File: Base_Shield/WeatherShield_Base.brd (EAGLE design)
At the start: 90.3 x 67.3 mm, 78 parts, among them Q1 BSS138, Q2 BSS138, U1 DS3231SN, U2 LT3652, U4 MPL3115A2LGA8, U5 HTU21D

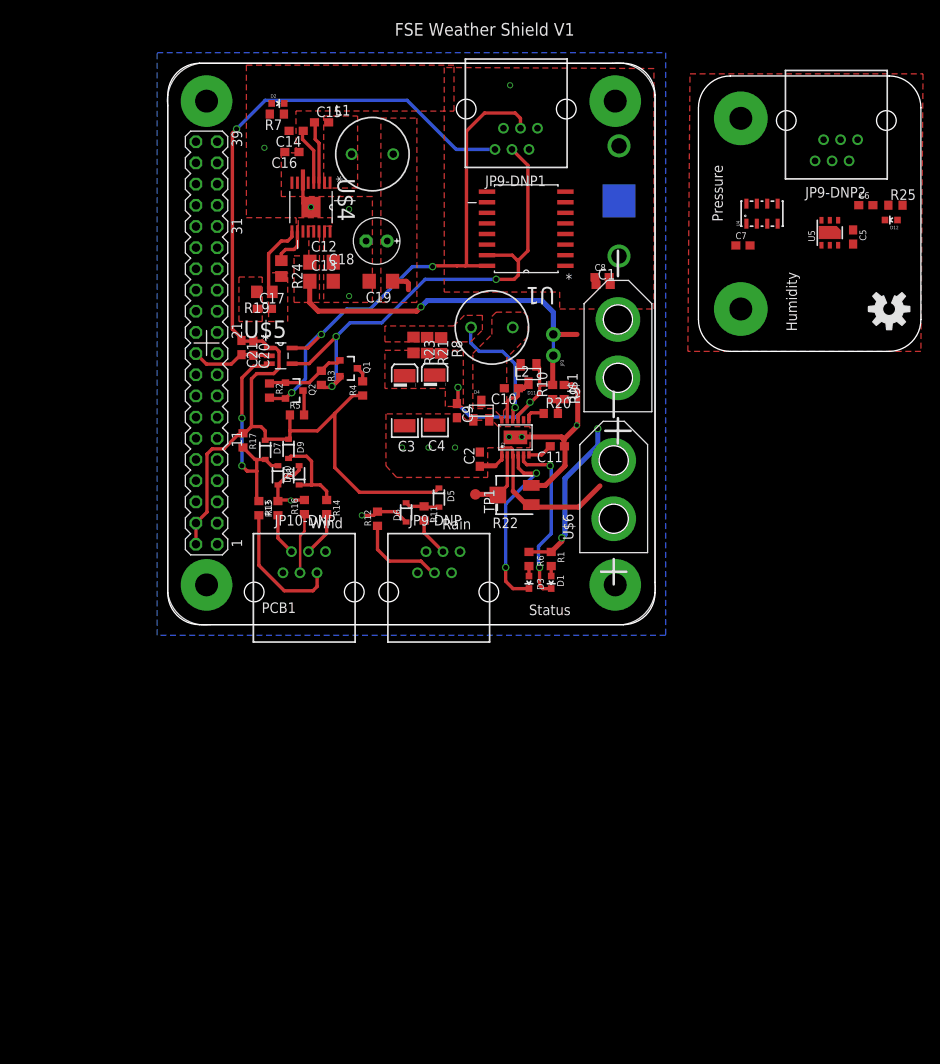
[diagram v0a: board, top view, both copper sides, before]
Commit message: WeatherShield v1
Restructuration des Fichiers
Division en Air et Base Board
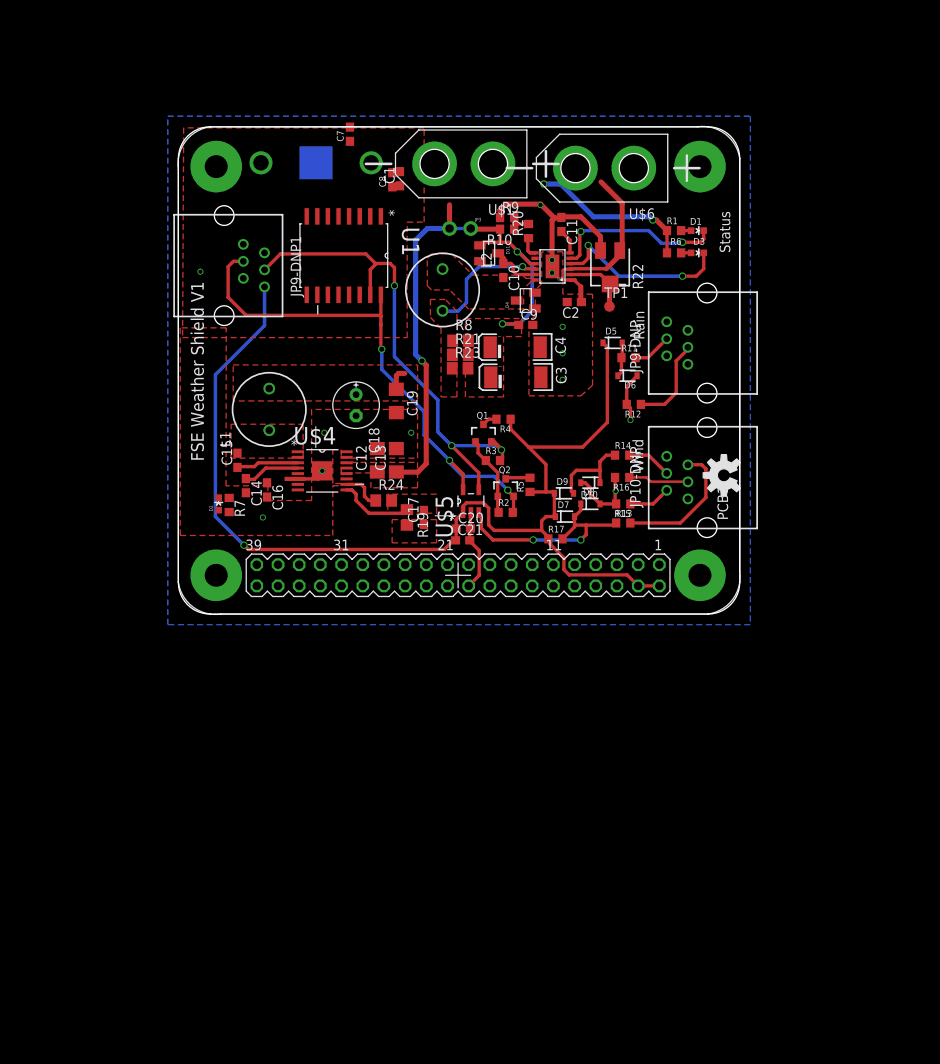
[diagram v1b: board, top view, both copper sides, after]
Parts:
- removed C5, C6: 0.1uF, rcl:C0603
- removed D12: AirBoard status led, SparkFun:LED-0603
- removed JP9-DNP2: RJ11-BUCHSE, FSEWeatherShield:RJ11-STECKER
- removed R25: 1K, rcl:R0603
- removed U4: MPL3115A2LGA8, SparkFun-Sensors:LGA8
- removed U5: HTU21D, SparkFun-Sensors:HTU21D
- moved JP10-DNP 61.9 mm to (70.7, 11.5), turned to 90 degrees
- moved PCB1 60.5 mm to (68.6, 59.7), turned to 180 degrees
- moved JP9-DNP 53.3 mm to (70.7, 27.7), turned to 90 degrees
- moved JP9-DNP1 50.7 mm to (0.76, 49.1), turned to 270 degrees
- moved C7 49.0 mm to (21.8, 58.8), turned to 90 degrees
- moved D2 48.5 mm to (6.10, 14.5), turned to 0 degrees
- moved R7 47.2 mm to (7.37, 14.4), turned to 270 degrees
- moved D1 45.7 mm to (63.5, 47.2), turned to 270 degrees
- moved D3 44.4 mm to (63.5, 44.6), turned to 270 degrees
- moved R13 43.7 mm to (54.6, 12.2), turned to 0 degrees
- moved C14 43.0 mm to (9.37, 16.7), turned to 270 degrees
- moved U$6 42.1 mm to (55.9, 54.7), turned to 180 degrees
- moved R1 42.0 mm to (60.7, 47.2), turned to 0 degrees
- moved C15 41.7 mm to (8.36, 19.7), turned to 90 degrees
- moved R15 41.4 mm to (54.6, 14.5), turned to 180 degrees
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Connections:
- removed net INT-PRESSURE: U4.6
- removed net N$28: D12.A, R25.2
- removed net N$5: C6.1, U4.2
- removed net STAT1: R25.1
- net 3.3V: no longer C5.1, JP9-DNP2.2, U4.1, U4.4, U5.VDD
- net 5V: no longer JP9-DNP2.1
- net GND: no longer C5.2, C6.2, D12.C, JP9-DNP2.5, JP9-DNP2.6, U4.3, U5.7, U5.GND
- net HV_SCL: now also PCB1.5
- net HV_SDA: now also PCB1.3
- net SCL: no longer JP9-DNP2.4, U4.8, U5.SCK
- net SDA: no longer JP9-DNP2.3, U4.7, U5.DATA
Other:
- board size 90.3 x 67.3 mm -> 67.3 x 58.4 mm
- board text removed: "Humidity"
- board text removed: "Pressure"

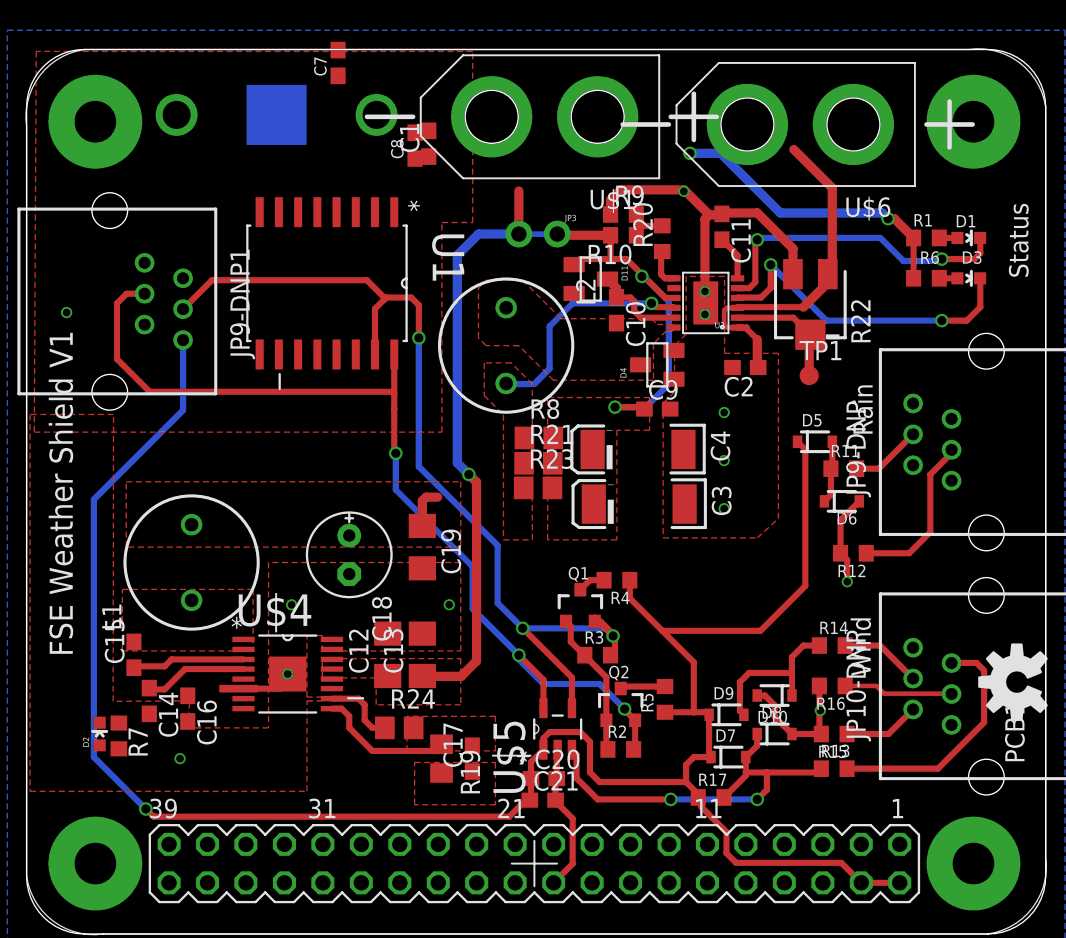
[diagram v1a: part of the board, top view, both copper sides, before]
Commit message: WeatherShield v1
First attempt almost done
GPIO routing is missing
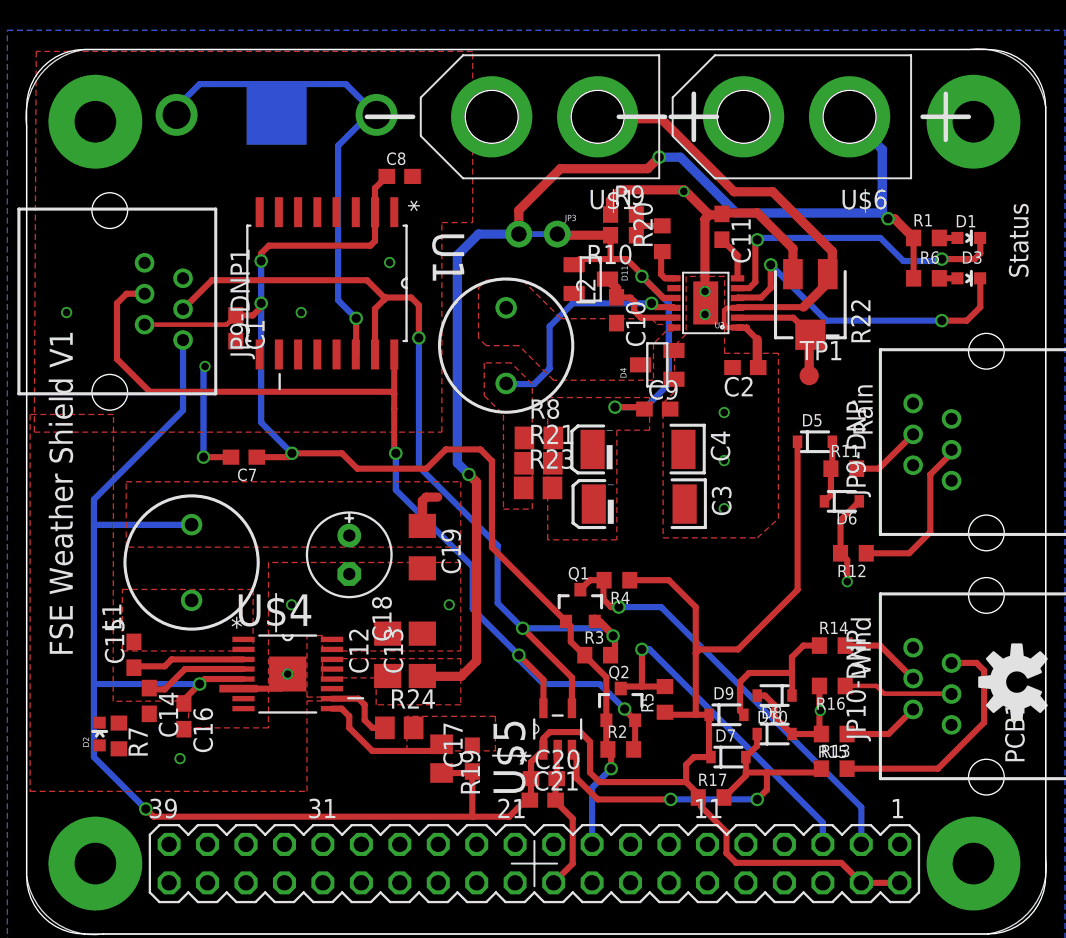
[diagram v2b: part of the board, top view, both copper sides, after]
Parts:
- moved C7 26.8 mm to (15.6, 32.8), turned to 180 degrees
- moved C1 17.6 mm to (15.1, 41.3), turned to 270 degrees
- moved C8 2.27 mm to (25.9, 51.3), turned to 0 degrees
- moved C16 0.57 mm to (11.7, 15.6)
- moved U$6 0.57 mm to (55.6, 55.2)
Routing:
- net 3.3V: track 9.63 -> 81.0 mm, vias 0 -> 4
- net N$6: track 0.00 -> 32.9 mm, vias 0 -> 1
- net HV_SDA: track 1.82 -> 28.3 mm, vias 0 -> 1
- net 5V: track 136.6 -> 159.4 mm, vias 1 -> 2
- net HV_SCL: track 2.98 -> 23.6 mm, vias 0 -> 1
- net V_BATT: track 58.6 -> 77.2 mm
- net VIN: track 23.4 -> 34.8 mm
- net GND: track 55.2 -> 63.1 mm, vias 13 -> 17
- added copper zone on layer 1, net 5V
- removed copper zone on layer 1, net +5V

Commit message: WeatherShield_v1
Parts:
- removed U$5: MCP3221A5T-E/OT, FSEWeatherShield:SOT95P270X145-5N
- added C5: 0.1uF, rcl:C0603
- added JP1, JP2, JP4: (no value), pinhead:1X02
- added JP5: (no value), pinhead:1X03
- added JP6, JP7, JP8: (no value), pinhead:1X01
- added U3: TMP100MDBVREP, FSEWeatherShield:SOT95P280X145-6N
- added U4: ADS1015IDGST, FSEWeatherShield:SOP50P490X110-10N
- moved C21 15.4 mm to (50.3, 13.7)
- moved R17 15.4 mm to (46.1, 25.7), turned to 270 degrees
- moved C20 14.9 mm to (50.3, 12.3)
- moved D7 14.5 mm to (51.8, 26.8), turned to 270 degrees
- moved R13 11.9 mm to (54.6, 24.1)
- moved D8 10.1 mm to (50.0, 24.5), turned to 270 degrees
- moved D9 7.38 mm to (48.0, 23.1), turned to 270 degrees
- moved R15 5.33 mm to (54.6, 19.8)
- moved R11 5.21 mm to (55.4, 37.2), turned to 90 degrees
- moved R5 4.85 mm to (43.9, 21.6)
- moved D10 4.78 mm to (51.6, 21.7), turned to 270 degrees
- moved R12 4.35 mm to (56.4, 30.7), turned to 90 degrees
- moved R16 3.81 mm to (54.6, 21.5)
- moved D6 3.57 mm to (55.4, 33.4)
- moved Q2 3.45 mm to (43.8, 17.4)
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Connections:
- new net N$14: JP6.1, U4.5
- new net N$18: JP4.1, PCB1.8
- new net N$19: JP4.2, PCB1.10
- new net N$20: JP5.3, PCB1.19
- new net N$21: JP5.2, PCB1.21
- new net N$25: JP5.1, PCB1.23
- new net N$8: JP7.1, U4.6
- new net N$9: JP8.1, U4.7
- net 3.3V: now also C5.1, JP2.1, U3.4
- net 5V: now also JP1.1, U4.8; no longer C20.1, C21.1, U$5.1
- net GND: now also C5.2, JP1.2, JP2.2, U3.2, U3.3, U3.5, U4.1, U4.3; no longer C20.2, C21.2, U$5.2
- net HV_SCL: now also U4.10; no longer PCB1.5
- net HV_SDA: now also U4.9; no longer PCB1.3
- net RAIN: now also PCB1.12
- net SCL: now also PCB1.5, U3.1; no longer U$5.5
- net SDA: now also PCB1.3, U3.6; no longer U$5.4
- net STAT3: now also PCB1.40
- net WDIR: now also U4.4; no longer U$5.3
- net WSPEED: now also PCB1.11
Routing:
- net SCL: track 64.1 -> 0.00 mm, vias 3 -> 0
- net SDA: track 63.2 -> 0.00 mm, vias 3 -> 0
- net 3.3V: track 81.0 -> 25.5 mm, vias 4 -> 0
- net RAIN: track 4.15 -> 55.1 mm, vias 0 -> 1
- net V_BATT: track 77.2 -> 41.2 mm, vias 3 -> 2
- net N$6: track 32.9 -> 0.00 mm, vias 1 -> 0
- net HV_SDA: track 28.3 -> 0.00 mm, vias 1 -> 0
- net GND: track 63.1 -> 39.4 mm, vias 17 -> 15
- net HV_SCL: track 23.6 -> 0.00 mm, vias 1 -> 0
- net 5V: track 159.4 -> 137.0 mm, vias 2 -> 1
- net STAT3: track 0.00 -> 12.8 mm, vias 0 -> 1
- net N$19: track 0.00 -> 12.5 mm
- net WSPEED: track 10.6 -> 23.0 mm
- net N$18: track 0.00 -> 10.1 mm
- net N$2: track 16.1 -> 9.85 mm
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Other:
- board text added: "Chrg"
- board text added: "Fault"
- board text removed: "Status"

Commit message: WeatherShield_v1
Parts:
- moved JP8 97.0 mm to (53.1, 18.3)
- moved JP7 91.7 mm to (50.5, 18.3)
- moved JP6 86.4 mm to (48.0, 18.3)
- moved U4 81.9 mm to (54.4, 14.5), turned to 90 degrees
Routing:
- net WDIR: track 20.5 -> 14.8 mm

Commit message: WeatherShield_v1
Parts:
- removed D10, D5, D6, D7, D8, D9: BAS16, SparkFun:SOD-323
- removed R11, R13, R15, R16: 1K, rcl:R0603
- R12, R14: value 1K -> 3k9
- R17: value 4.7K -> 10k
- moved R12 93.3 mm to (-16.8, -27.2), turned to 0 degrees
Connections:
- removed net N$1: JP10-DNP.3, R14.2
- removed net N$11: JP9-DNP.4, R12.1
- removed net N$12: JP10-DNP.5, R15.1
- removed net N$13: JP10-DNP.4, R16.1
- removed net N$2: JP10-DNP.2, R13.2
- removed net N$4: JP9-DNP.3, R11.2
- removed net RAIN2: JP9-DNP.2
- removed net RAIN5: JP9-DNP.5
- net 3.3V: now also JP10-DNP.3, JP9-DNP.3
- net 5V: no longer D5.1, D7.1, D9.1
- net GND: now also JP10-DNP.5, R14.2; no longer D10.2, D6.2, D8.2, R15.2, R16.2
- net RAIN: now also JP9-DNP.4, R12.1; no longer D5.2, D6.1, R11.1
- net WDIR: now also JP10-DNP.2; no longer D7.2, D8.1, R13.1
- net WSPEED: now also JP10-DNP.4; no longer D10.1, D9.2
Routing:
- net 5V: track 137.0 -> 123.9 mm
- net N$13: track 10.3 -> 0.00 mm
- net N$2: track 9.85 -> 0.00 mm
- net GND: track 39.4 -> 30.4 mm, vias 15 -> 13
- net N$11: track 8.73 -> 0.00 mm
- net N$1: track 7.96 -> 0.00 mm
- net N$4: track 7.24 -> 0.00 mm
- net N$12: track 7.07 -> 0.00 mm
- net WDIR: track 14.8 -> 8.42 mm
- net WSPEED: track 23.0 -> 16.7 mm
- net RAIN: track 55.1 -> 49.9 mm

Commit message: WeatherShield_v1
routing....
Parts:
- added C6: 0.1uF, rcl:C0603
- moved R12 96.8 mm to (55.6, 37.1), turned to 90 degrees
- moved C21 41.1 mm to (16.0, 36.1), turned to 180 degrees
- moved U4 15.1 mm to (52.3, 29.5), turned to 270 degrees
- moved C1 14.0 mm to (27.8, 47.1), turned to 90 degrees
- moved JP6 11.0 mm to (38.4, 23.6)
- moved JP7 11.0 mm to (40.9, 23.6)
- moved R4 11.0 mm to (41.5, 13.7)
- moved JP8 10.8 mm to (43.7, 23.6)
- moved R17 10.1 mm to (55.8, 28.7), turned to 90 degrees
- moved C7 9.92 mm to (25.5, 32.3), turned to 0 degrees
- moved R2 8.33 mm to (51.8, 15.9), turned to 90 degrees
- moved R3 6.82 mm to (44.3, 17.4), turned to 90 degrees
- moved Q1 6.29 mm to (41.1, 17.5), turned to 90 degrees
- moved Q2 4.10 mm to (47.6, 15.9), turned to 90 degrees
- moved R5 3.61 mm to (46.7, 19.3), turned to 0 degrees
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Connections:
- net 5V: now also C6.1
- net GND: now also C6.2
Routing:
- net 3.3V: track 25.5 -> 116.4 mm, vias 0 -> 2
- net SCL: track 0.00 -> 62.7 mm, vias 0 -> 2
- net SDA: track 0.00 -> 48.5 mm
- net N$6: track 0.00 -> 37.6 mm, vias 0 -> 1
- net HV_SCL: track 0.00 -> 27.5 mm
- net N$14: track 0.00 -> 17.7 mm
- net 5V: track 123.9 -> 139.4 mm
- net WDIR: track 8.42 -> 21.6 mm, vias 2 -> 0
- net N$8: track 0.00 -> 13.0 mm
- net RAIN: track 49.9 -> 61.7 mm
- net N$9: track 0.00 -> 10.4 mm
- net HV_SDA: track 0.00 -> 9.16 mm, vias 0 -> 1
- net WSPEED: track 16.7 -> 10.9 mm
- net GND: vias 13 -> 8

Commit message: WeatherShield_v1
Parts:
- removed C20, C21: 0.1uF, rcl:C0603
- removed LOGO1: OSHW-LOGOM, SparkFun-Aesthetics:OSHW-LOGO-M
- moved JP6 15.3 mm to (49.0, 34.5)
- moved JP7 10.0 mm to (49.0, 29.5)
- moved JP8 9.94 mm to (49.0, 32.0)
- moved R4 8.21 mm to (42.7, 21.8), turned to 0 degrees
- moved R14 8.13 mm to (55.6, 13.0)
- moved C7 8.07 mm to (18.4, 36.1)
- moved R3 7.47 mm to (50.4, 21.7)
- moved Q1 7.26 mm to (46.9, 21.8)
- moved U3 5.64 mm to (36.3, 21.6), turned to 270 degrees
- moved R5 5.00 mm to (42.7, 16.4)
- moved R12 3.09 mm to (56.1, 34.0)
- moved C5 1.63 mm to (36.3, 17.8), turned to 0 degrees
- moved R2 1.37 mm to (50.5, 16.4)
- moved Q2 1.02 mm to (46.7, 16.4)
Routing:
- net 3.3V: track 116.4 -> 187.9 mm, vias 2 -> 3
- net V_BATT: track 41.2 -> 77.8 mm, vias 2 -> 3
- net SDA: track 48.5 -> 77.6 mm, vias 0 -> 1
- net 5V: track 139.4 -> 159.6 mm, vias 1 -> 5
- net N$14: track 17.7 -> 4.46 mm
- net WSPEED: track 10.9 -> 23.4 mm
- net SCL: track 62.7 -> 73.9 mm, vias 2 -> 3
- net RAIN: track 61.7 -> 50.7 mm
- net N$8: track 13.0 -> 3.74 mm
- net HV_SCL: track 27.5 -> 21.3 mm, vias 0 -> 2
- net N$9: track 10.4 -> 6.03 mm
- net HV_SDA: track 9.16 -> 13.6 mm, vias 1 -> 0
- net N$19: track 12.5 -> 11.7 mm
- net GND: vias 8 -> 9
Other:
- board text added: "Pwr"

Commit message: WeatherShield_v1
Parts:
- moved PCB1 68.0 mm to (1.14, 68.3), turned to 270 degrees
- moved JP10-DNP 62.6 mm to (49.3, 70.4), turned to 180 degrees
- moved JP9-DNP 56.9 mm to (33.2, 70.4), turned to 180 degrees
- moved D1 52.4 mm to (13.6, 63.2), turned to 0 degrees
- moved D3 50.8 mm to (16.3, 63.2), turned to 0 degrees
- moved U$6 50.0 mm to (5.59, 55.4), turned to 270 degrees
- moved JP9-DNP1 49.9 mm to (11.7, 0.51), turned to 0 degrees
- moved R1 48.9 mm to (13.6, 60.5), turned to 90 degrees
- moved R6 47.2 mm to (16.3, 60.5), turned to 90 degrees
- moved R14 43.1 mm to (47.9, 55.4), turned to 0 degrees
- moved D2 41.3 mm to (45.3, 5.08), turned to 90 degrees
- moved R7 40.8 mm to (47.0, 6.60), turned to 180 degrees
- moved G1 39.8 mm to (5.46, 17.5), turned to 270 degrees
- moved C6 39.3 mm to (35.4, 57.7), turned to 90 degrees
- moved U$1 37.3 mm to (5.59, 38.7), turned to 270 degrees
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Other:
- board size 67.3 x 58.4 mm -> 58.4 x 67.3 mm
